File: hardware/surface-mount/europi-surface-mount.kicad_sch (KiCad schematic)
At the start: 88 parts, among them J1 Conn_02x05_Odd_Even, J10 Output 6 Jack, J11 Conn_01x04_Pin, J2 Conn_01x04_Pin, J3 Output 1 Jack, J4 Output 4 Jack, J5 Analogue Input Jack, J6 Output 2 Jack, J7 Output 5 Jack, J8 Digital Input Jack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

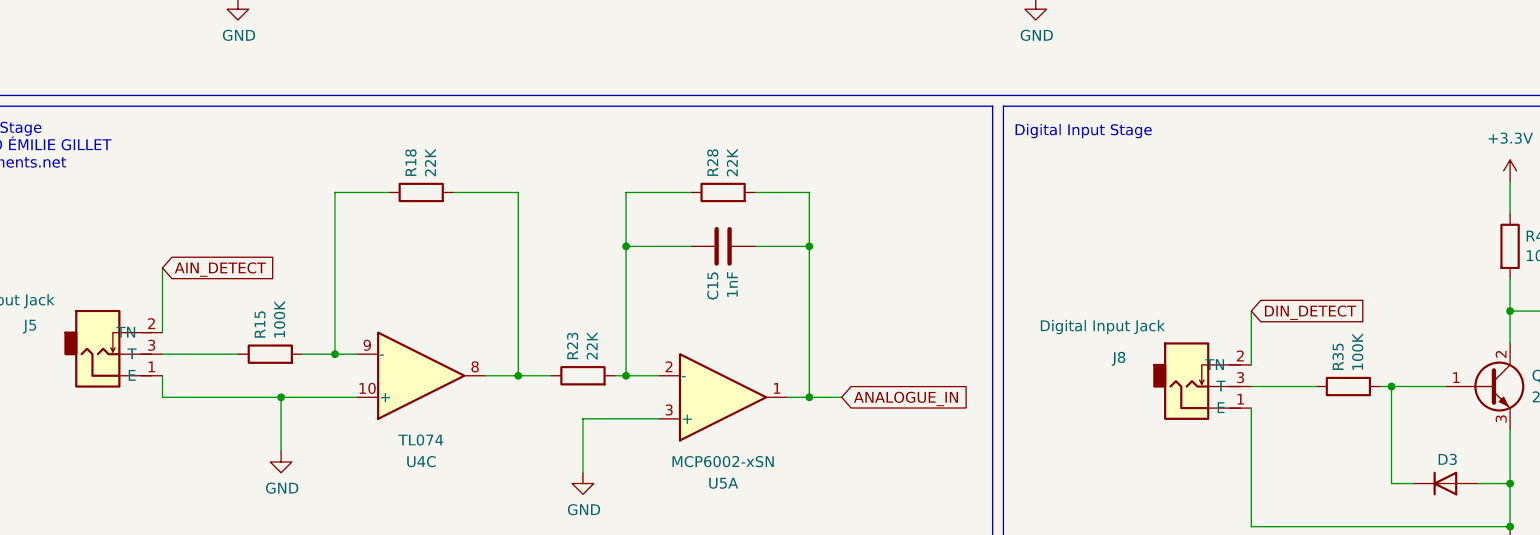
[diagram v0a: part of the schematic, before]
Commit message: add resistors to input detect and add oshwa cert mark
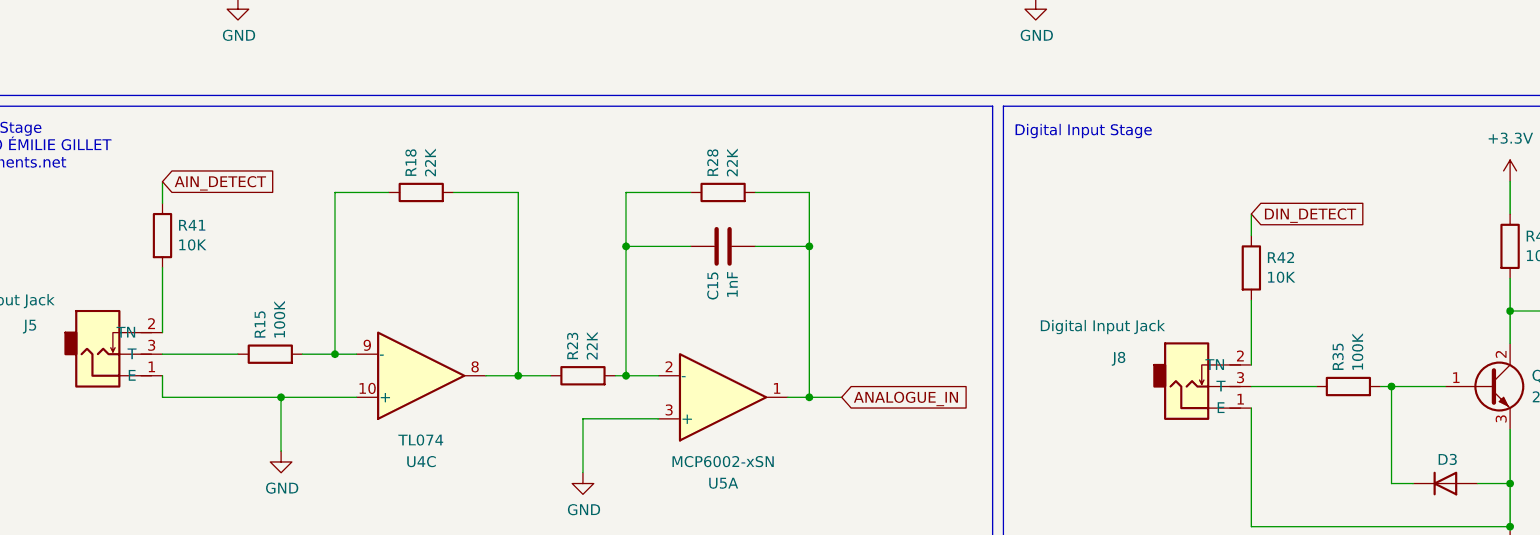
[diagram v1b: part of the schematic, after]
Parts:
- added R41, R42: 10K, Resistor_SMD:R_0603_1608Metric, symbol Device:R
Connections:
- net AIN_DETECT: now also R41.1; no longer J5.2 (TN)
- net DIN_DETECT: now also R42.1; no longer J8.2 (TN)
- new net: J8.2 (TN), R42.2
- new net: J5.2 (TN), R41.2
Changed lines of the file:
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@@
 	(wire
 		(pts
-			(xy 254 167.64) (xy 254 173.99)
+			(xy 254 166.37) (xy 254 173.99)
 		)
 		(stroke
@@
 	(wire
 		(pts
+			(xy 125.73 152.4) (xy 125.73 154.94)
+		)
+		(stroke
+			(width 0)
+			(type default)
+		)
+	)
+	(wire
+		(pts
 			(xy 134.62 74.93) (xy 134.62 69.85)
 		)
@@
 	(wire
 		(pts
+			(xy 254 156.21) (xy 254 158.75)
+		)
+		(stroke
+			(width 0)
+			(type default)
+		)
+	)
+	(wire
+		(pts
 			(xy 339.09 110.49) (xy 335.28 110.49)
 		)
@@
 	(global_label "AIN_DETECT"
 		(shape input)
-		(at 125.73 162.56 0)
+		(at 125.73 152.4 0)
 		(fields_autoplaced yes)
 		(effects
@@
 		)
 		(property "Intersheetrefs" "${INTERSHEET_REFS}"
-			(at 139.4799 162.56 0)
+			(at 139.4799 152.4 0)
 			(effects
 				(font
@@
 	(global_label "DIN_DETECT"
 		(shape input)
-		(at 254 167.64 0)
+		(at 254 156.21 0)
 		(fields_autoplaced yes)
 		(effects
@@
 		)
 		(property "Intersheetrefs" "${INTERSHEET_REFS}"
-			(at 267.9313 167.64 0)
+			(at 267.9313 156.21 0)
 			(effects
 				(font
@@
 	)
 	(symbol
+		(lib_id "Device:R")
+		(at 125.73 158.75 0)
+		(unit 1)
+		(exclude_from_sim no)
+		(in_bom yes)
+		(on_board yes)
+		(dnp no)
+		(property "Reference" "R41"
+			(at 127.508 157.5816 0)
+			(effects
+				(font
+					(size 1.27 1.27)
+				)
+				(justify left)
+			)
+		)
+		(property "Value" "10K"
+			(at 127.508 159.893 0)
+			(effects
+				(font
+					(size 1.27 1.27)
+				)
+				(justify left)
+			)
+		)
+		(property "Footprint" "Resistor_SMD:R_0603_1608Metric"
+			(at 123.952 158.75 90)
+			(effects
+				(font
+					(size 1.27 1.27)
+				)
+				(hide yes)
+			)
+		)
+		(property "Datasheet" "~"
+			(at 125.73 158.75 0)
+			(effects
+				(font
+					(size 1.27 1.27)
+				)
+				(hide yes)
+			)
+		)
+		(property "Description" ""
+			(at 125.73 158.75 0)
+			(effects
+				(font
+					(size 1.27 1.27)
+				)
+			)
+		)
+		(pin "1"
+		)
+		(pin "2"
+		)
+		(instances
+			(project "europi-surface-mount"
+				(path "/5701b80f-f006-4814-81c9-0c7f006088a9"
+					(reference "R41")
+					(unit 1)
+				)
+			)
+		)
+	)
+	(symbol
 		(lib_id "power:GND")
 		(at 328.93 189.23 270)
@@
 					(unit 1)
 				)
+			)
+		)
+	)
+	(symbol
+		(lib_id "Device:R")
+		(at 254 162.56 0)
+		(unit 1)
+		(exclude_from_sim no)
+		(in_bom yes)
+		(on_board yes)
+		(dnp no)
+		(property "Reference" "R42"
+			(at 255.778 161.3916 0)
+			(effects
+				(font
+					(size 1.27 1.27)
+				)
+				(justify left)
+			)
+		)
+		(property "Value" "10K"
+			(at 255.778 163.703 0)
+			(effects
+				(font
+					(size 1.27 1.27)
+				)
+				(justify left)
+			)
+		)
+		(property "Footprint" "Resistor_SMD:R_0603_1608Metric"
+			(at 252.222 162.56 90)
+			(effects
+				(font
+					(size 1.27 1.27)
+				)
+				(hide yes)
+			)
+		)
+		(property "Datasheet" "~"
+			(at 254 162.56 0)
+			(effects
+				(font
+					(size 1.27 1.27)
+				)
+				(hide yes)
+			)
+		)
+		(property "Description" ""
+			(at 254 162.56 0)
+			(effects
+				(font
+					(size 1.27 1.27)
+				)
+			)
+		)
+		(pin "1"
+		)
+		(pin "2"
+		)
+		(instances
+			(project "europi-surface-mount"
+				(path "/5701b80f-f006-4814-81c9-0c7f006088a9"
+					(reference "R42")
+					(unit 1)
+				)
